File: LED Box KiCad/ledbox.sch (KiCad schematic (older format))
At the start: 34 parts, among them CON1 AVR_ISP, J1 Power, J2 Bus, J3 IR LED, J4 Button, U1 ATTINY2313-20PU, U2 ST485C, U3 ULN2003, Y1 DNP/20MHz

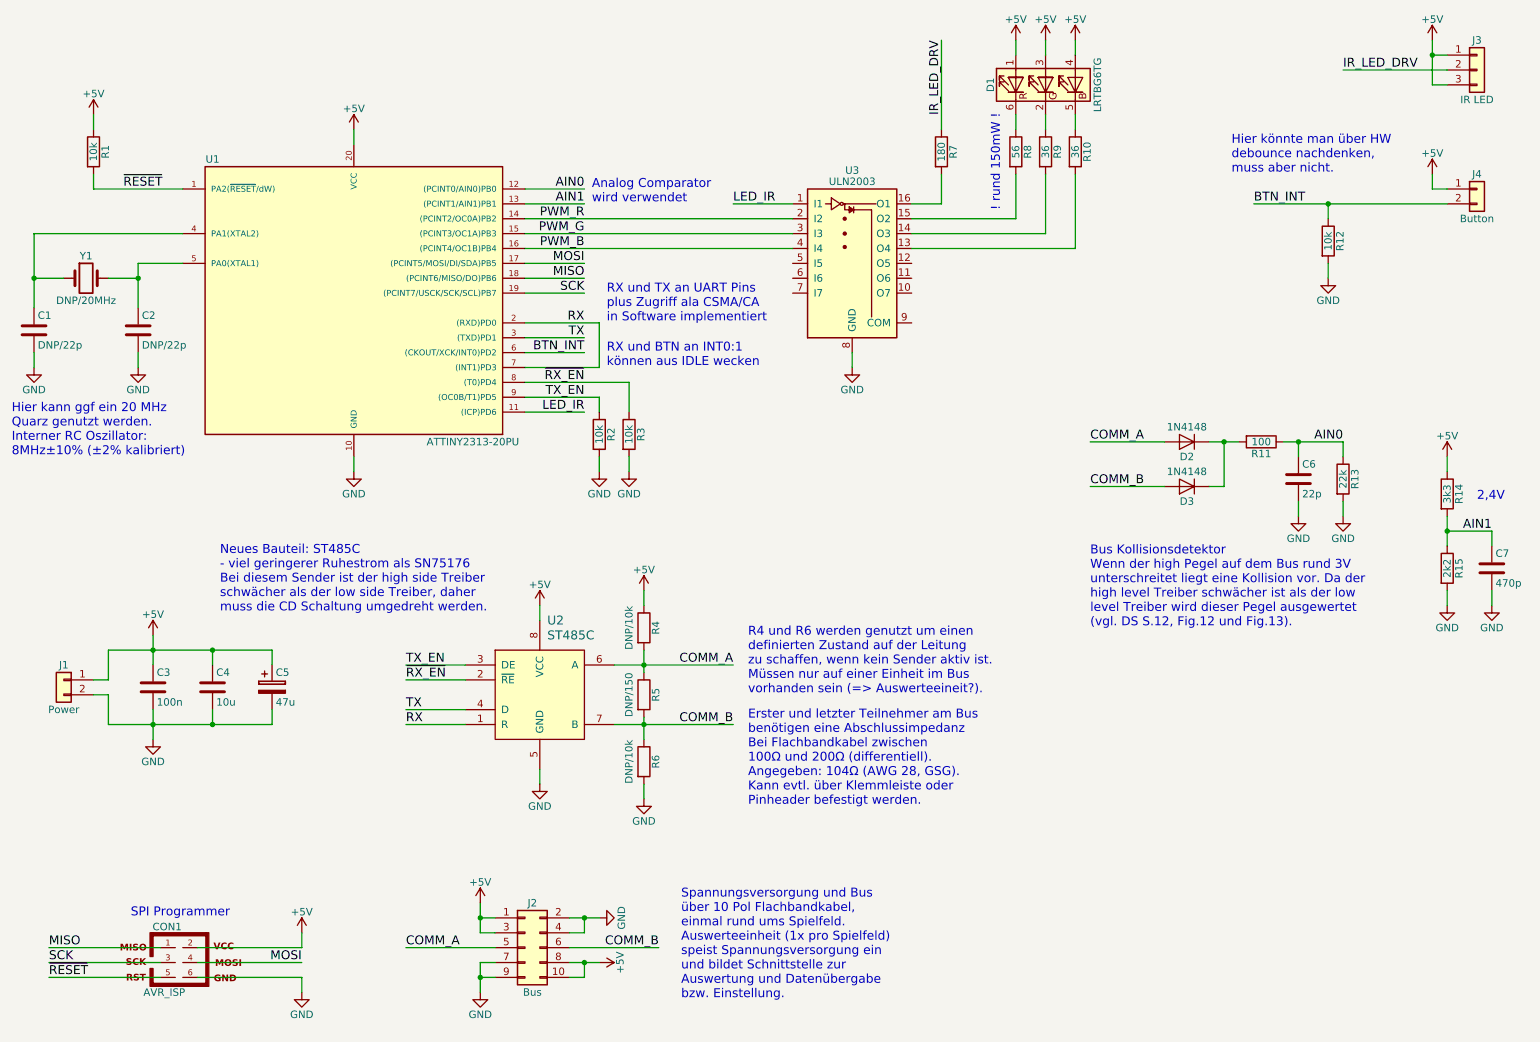
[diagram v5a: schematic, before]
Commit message: Version 3: - ATmega88 - Schaltplan auf verschiedene sheets aufgeteilt - div. kleine Änderungen
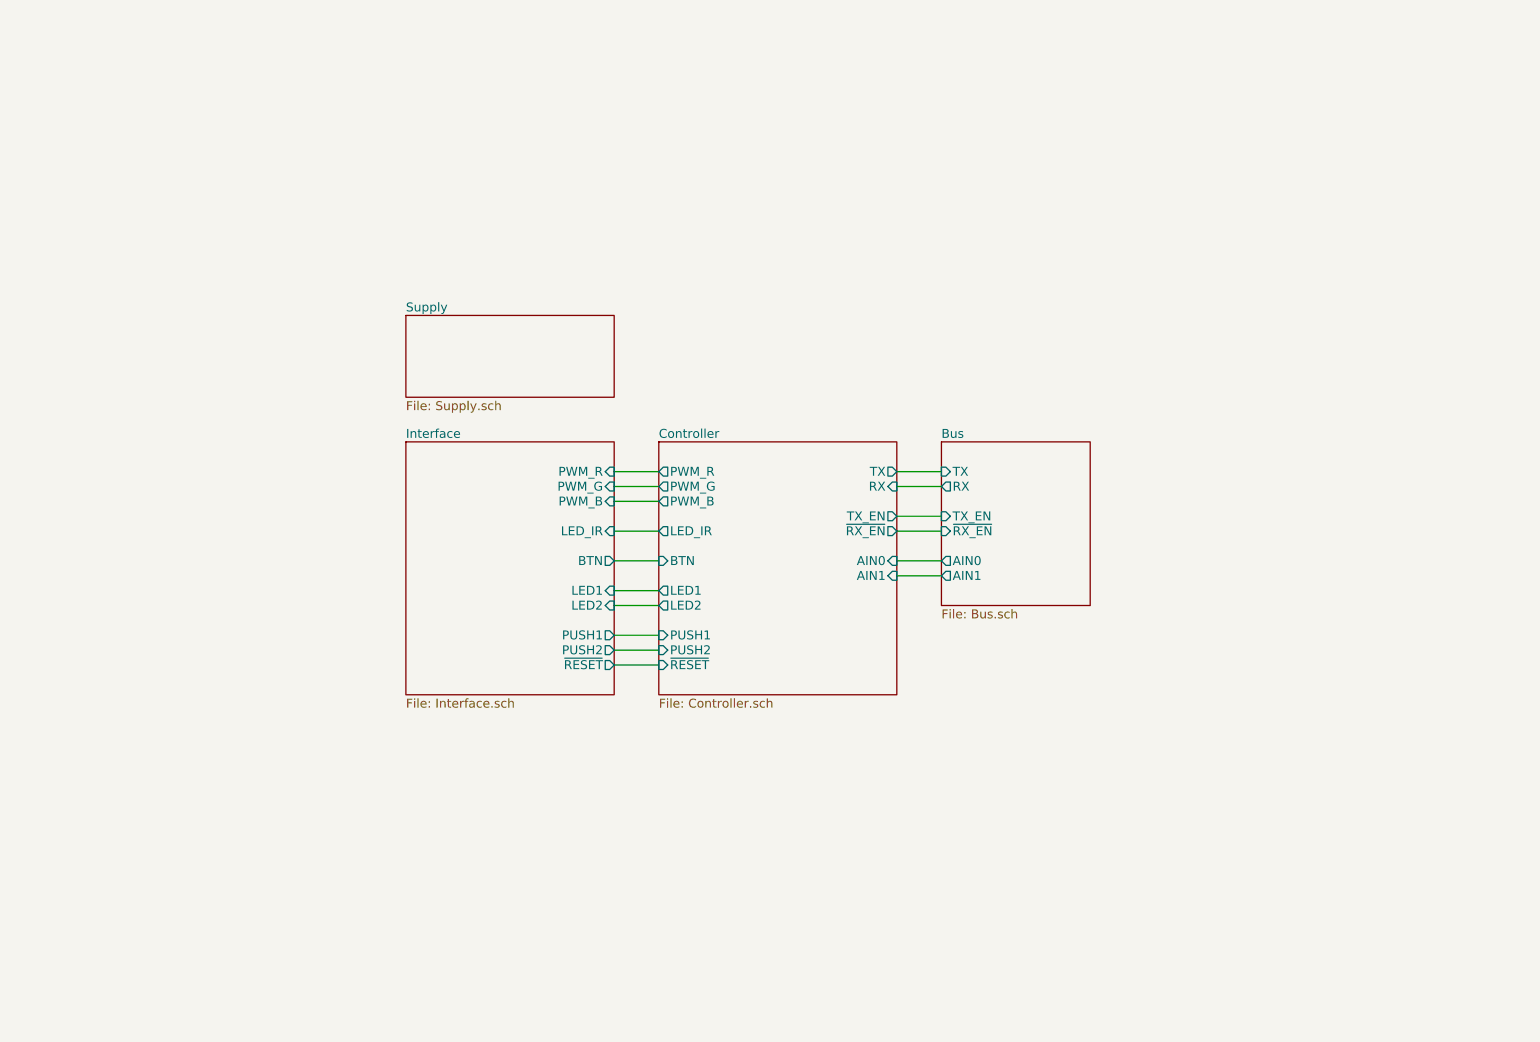
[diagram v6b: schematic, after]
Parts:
- removed C1, C2: DNP/22p, Capacitors_SMD:C_1206, symbol C
- removed C3: 100n, Capacitors_SMD:C_1206, symbol C
- removed C4: 10u, Capacitors_SMD:C_1206, symbol C
- removed C5: 47u, Capacitors_SMD:CP_Elec_4x5.7, symbol CP
- removed C6: 22p, Capacitors_SMD:C_1206, symbol C
- removed C7: 470p, Capacitors_SMD:C_1206, symbol C
- removed CON1: AVR_ISP, Pin_Headers:Pin_Header_Straight_2x03, symbol AVR-ISP-6
- removed D1: LRTBG6TG, ledbox-newfootprints:LED-6-BIG, symbol LRTBG6TG
- removed D2, D3: 1N4148, Diodes_SMD:D_MiniMELF, symbol D
- removed J1: Power, Connectors_Terminal_Blocks:TerminalBlock_Pheonix_MKDS1.5-2pol, symbol Conn_01x02
- removed J2: Bus, Pin_Headers:Pin_Header_Straight_2x05, symbol Conn_02x05_Odd_Even
- removed J3: IR LED, Pin_Headers:Pin_Header_Straight_1x03, symbol Conn_01x03
- removed J4: Button, Pin_Headers:Pin_Header_Straight_1x02, symbol Conn_01x02
- removed R1, R12, R2, R3: 10k, Resistors_SMD:R_1206, symbol R
- removed R10, R9: 36, Resistors_SMD:R_1206, symbol R
- removed R11: 100, Resistors_SMD:R_1206, symbol R
- removed R13: 22k, Resistors_SMD:R_1206, symbol R
- removed R14: 3k3, Resistors_SMD:R_1206, symbol R
- removed R15: 2k2, Resistors_SMD:R_1206, symbol R
- removed R4, R6: DNP/10k, Resistors_SMD:R_1206, symbol R
- removed R5: DNP/150, Resistors_SMD:R_1206, symbol R
- removed R7: 180, Resistors_SMD:R_1206, symbol R
- removed R8: 56, Resistors_SMD:R_1206, symbol R
- removed U1: ATTINY2313-20PU, Housings_SOIC:SOIC-20W_7.5x12.8mm_Pitch1.27mm, symbol ATTINY2313-20PU
- removed U2: ST485C, Housings_SOIC:SOIC-8_3.9x4.9mm_Pitch1.27mm, symbol SN75176B
- removed U3: ULN2003, Housings_SOIC:SOIC-16_3.9x9.9mm_Pitch1.27mm, symbol ULN2003
- removed Y1: DNP/20MHz, Crystals:Crystal_HC49-SD_SMD, symbol Crystal
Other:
- note removed: "! rund 150mW !"
- note removed: "2,4V"
- note removed: "Analog Comparator \nwird verwendet"
- note removed: "Bus Kollisionsdetektor\nWenn der high Pegel auf dem Bus rund 3V \nunterschreitet liegt eine Kollision vor. Da der \nhigh level Treiber schwächer ist als der low \nlevel Treiber wird dieser Pegel ausgewertet \n(vgl. DS S.12, Fig.12 und Fig.13)."
- note removed: "Erster und letzter Teilnehmer am Bus \nbenötigen eine Abschlussimpedanz\nBei Flachbandkabel zwischen \n100Ω und 200Ω (differentiell).\nAngegeben: 104Ω (AWG 28, GSG).\nKann evtl. über Klemmleiste oder\nPinheader befestigt werden."
- note removed: "Hier kann ggf ein 20 MHz \nQuarz genutzt werden.\nInterner RC Oszillator: \n8MHz±10% (±2% kalibriert)"
- note removed: "Hier könnte man über HW \ndebounce nachdenken, \nmuss aber nicht."
- note removed: "Neues Bauteil: ST485C \n- viel geringerer Ruhestrom als SN75176 \nBei diesem Sender ist der high side Treiber \nschwächer als der low side Treiber, daher \nmuss die CD Schaltung umgedreht werden.\n"
- note removed: "R4 und R6 werden genutzt um einen \ndefinierten Zustand auf der Leitung \nzu schaffen, wenn kein Sender aktiv ist.\nMüssen nur auf einer Einheit im Bus \nvorhanden sein (=> Auswerteeineit?)."
- note removed: "RX und BTN an INT0:1\nkönnen aus IDLE wecken"
- note removed: "RX und TX an UART Pins\nplus Zugriff ala CSMA/CA\nin Software implementiert"
- note removed: "SPI Programmer"
- note removed: "Spannungsversorgung und Bus \nüber 10 Pol Flachbandkabel, \neinmal rund ums Spielfeld. \nAuswerteeinheit (1x pro Spielfeld) \nspeist Spannungsversorgung ein \nund bildet Schnittstelle zur \nAuswertung und Datenübergabe\nbzw. Einstellung."

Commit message: Board Layout (SMD) fertiggestellt
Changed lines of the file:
@@
 F3 "AIN1" O L 6900 4500 60
 F4 "TX_EN" I L 6900 4100 60
-F5 "~RX_EN" I L 6900 4200 60
-F6 "TX" I L 6900 3800 60
-F7 "RX" O L 6900 3900 60
+F5 "TX" I L 6900 3800 60
+F6 "RX" O L 6900 3900 60
 $EndSheet
 $Sheet
@@
 F3 "PWM_G" O L 5000 3900 60
 F4 "TX_EN" O R 6600 4100 60
-F5 "~RX_EN" O R 6600 4200 60
-F6 "RX" I R 6600 3900 60
-F7 "TX" O R 6600 3800 60
-F8 "PWM_B" O L 5000 4000 60
-F9 "BTN" I L 5000 4400 60
-F10 "LED_IR" O L 5000 4200 60
-F11 "AIN0" I R 6600 4400 60
-F12 "AIN1" I R 6600 4500 60
-F13 "LED1" O L 5000 4600 60
-F14 "LED2" O L 5000 4700 60
-F15 "PUSH1" I L 5000 4900 60
-F16 "PUSH2" I L 5000 5000 60
-F17 "~RESET" I L 5000 5100 60
+F5 "RX" I R 6600 3900 60
+F6 "TX" O R 6600 3800 60
+F7 "PWM_B" O L 5000 4000 60
+F8 "BTN" I L 5000 4400 60
+F9 "LED_IR" O L 5000 4200 60
+F10 "AIN0" I R 6600 4400 60
+F11 "AIN1" I R 6600 4500 60
+F12 "LED1" O L 5000 4600 60
+F13 "LED2" O L 5000 4700 60
+F14 "PUSH1" I L 5000 4900 60
+F15 "PUSH2" I L 5000 5000 60
+F16 "~RESET" I L 5000 5100 60
 $EndSheet
 $Sheet
@@
 	6900 4100 6600 4100
 Wire Wire Line
-	6600 4200 6900 4200
-Wire Wire Line
 	6900 4400 6600 4400
